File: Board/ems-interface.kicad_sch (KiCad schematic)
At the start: 51 parts, among them J8 EMS, Q1 BC858, Q11 BC848, U2 LM393, U3 MP1584

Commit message: Minor fixes
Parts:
- C11: value 22u -> 47u
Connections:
- net BUCK_EN: now reaches R15.1, R16.2, U3.2 (EN)
- net BUCK_FREQ: now reaches R13.1, U3.6 (FREQ)
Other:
- note added: "3.3 V"
- moved on the sheet: C10, C11, C12, C13, C9, D10, L3, R13, R14, R17, R18, U3

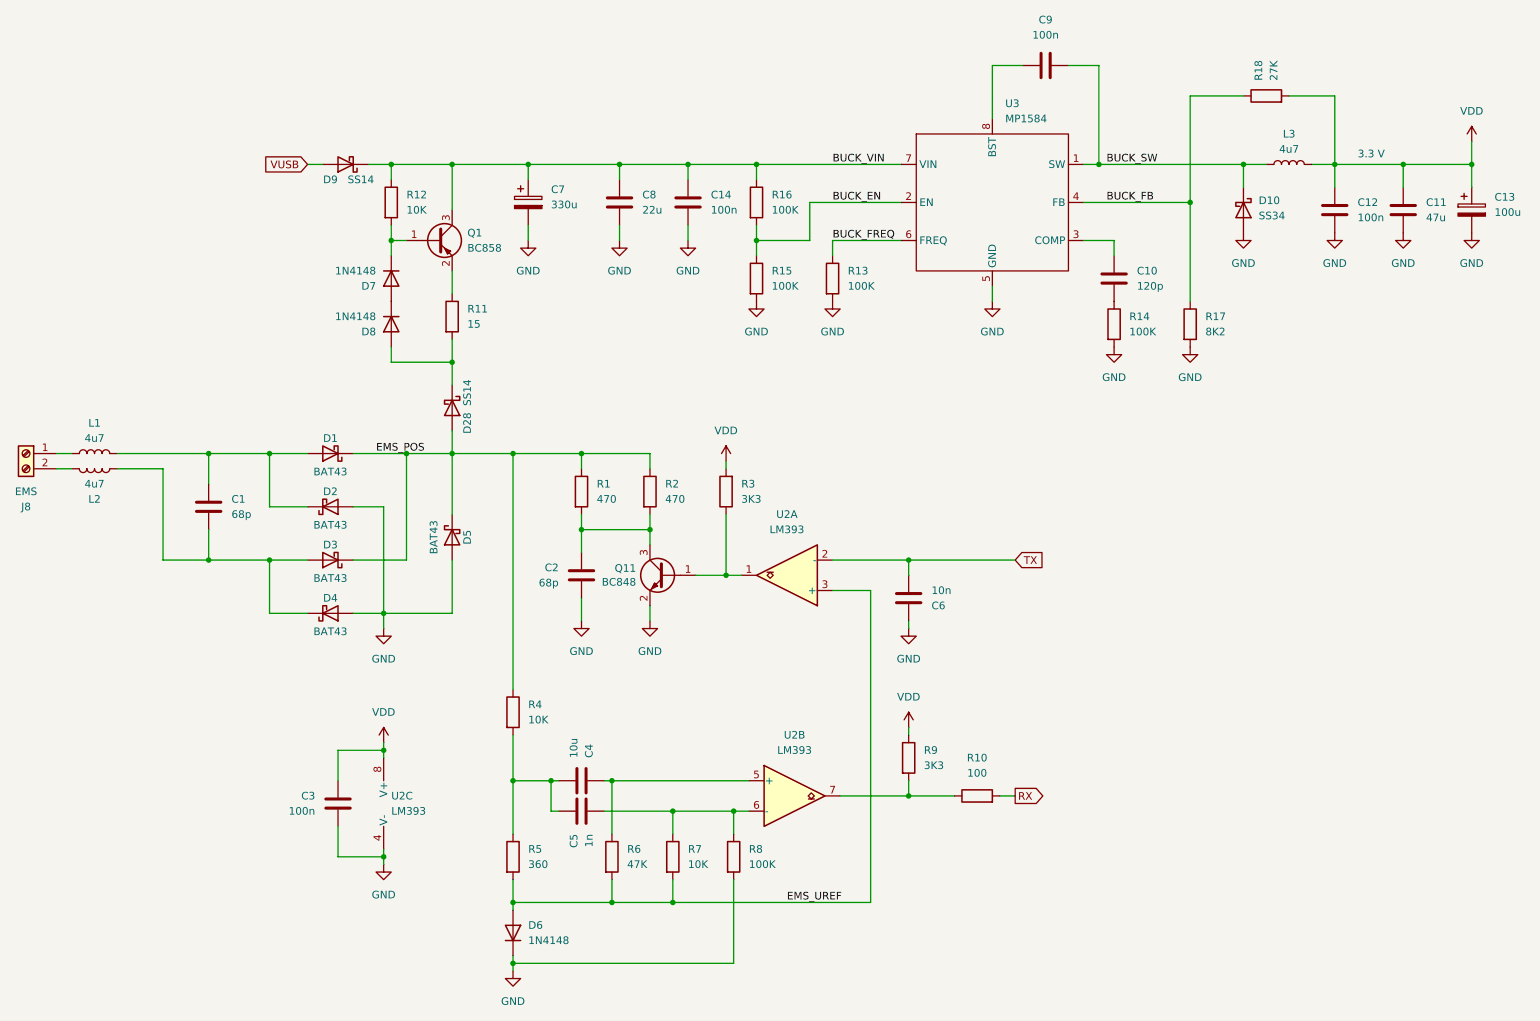
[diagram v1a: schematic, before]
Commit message: Fixes values
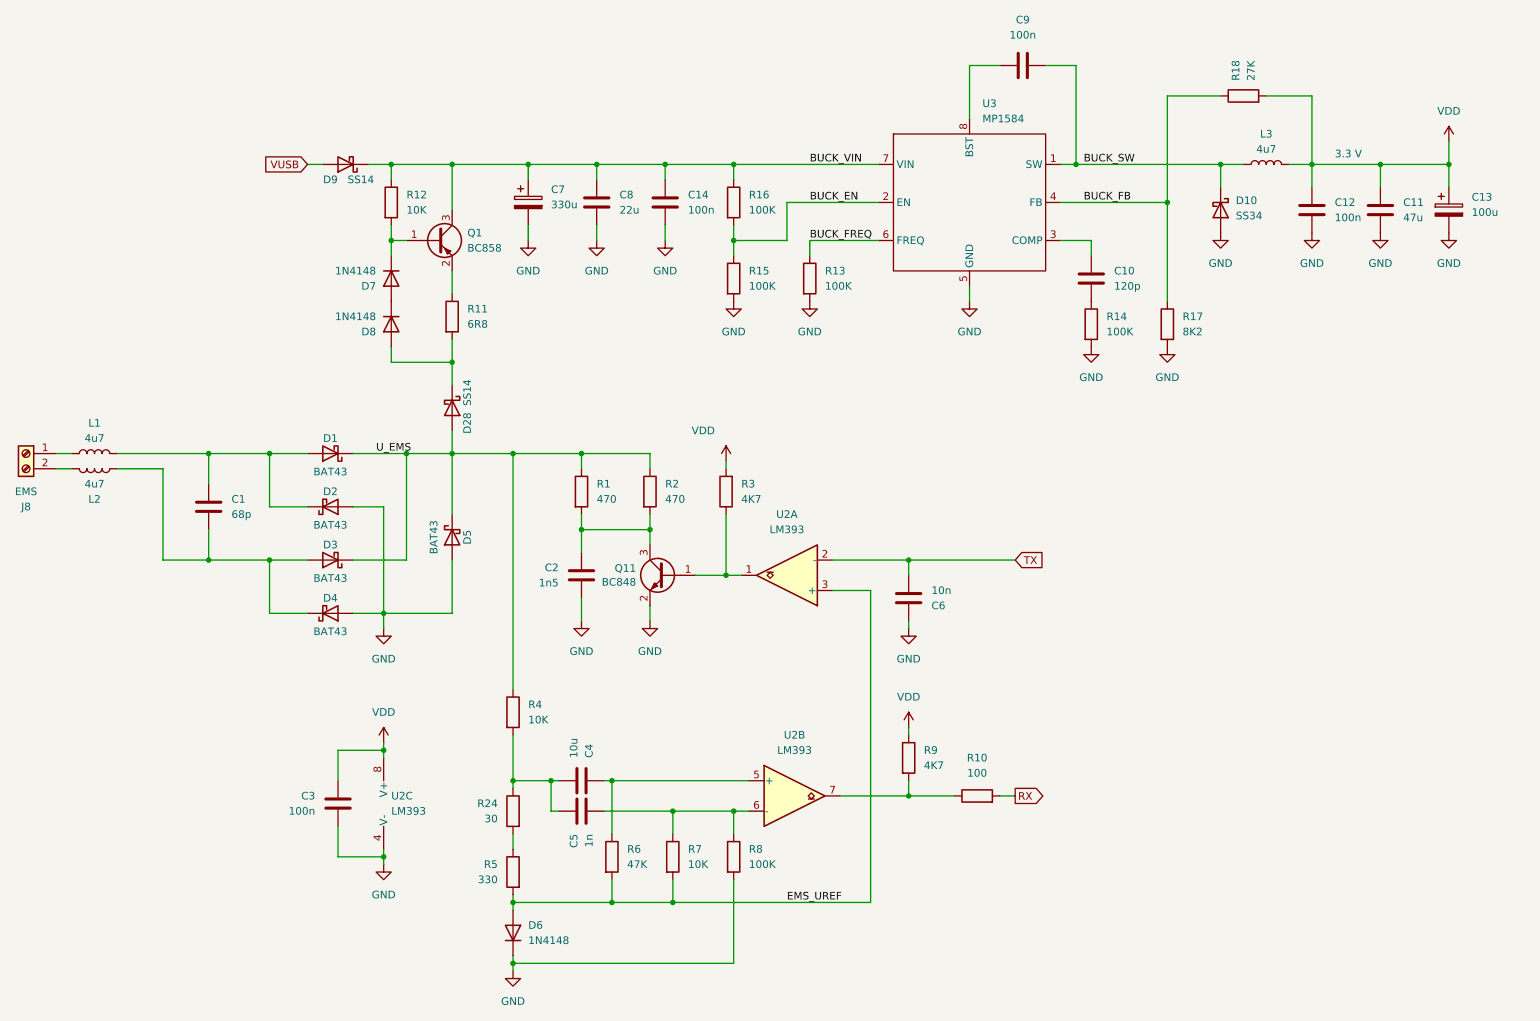
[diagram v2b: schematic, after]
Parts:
- added R24: 30, Resistor_SMD:R_0805_2012Metric, symbol Device:R
- C2: value 68p -> 1n5
- R11: value 15 -> 6R8
- R3, R9: value 3K3 -> 4K7
- R5: value 360 -> 330
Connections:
- net at C4.2, C5.1, R4.2: now also R24.1; no longer R5.1
- net EMS_POS renamed U_EMS
- new net: R24.2, R5.1
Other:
- moved on the sheet: C10, C11, C12, C13, C14, C8, C9, D10, L3, R13, R14, R15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

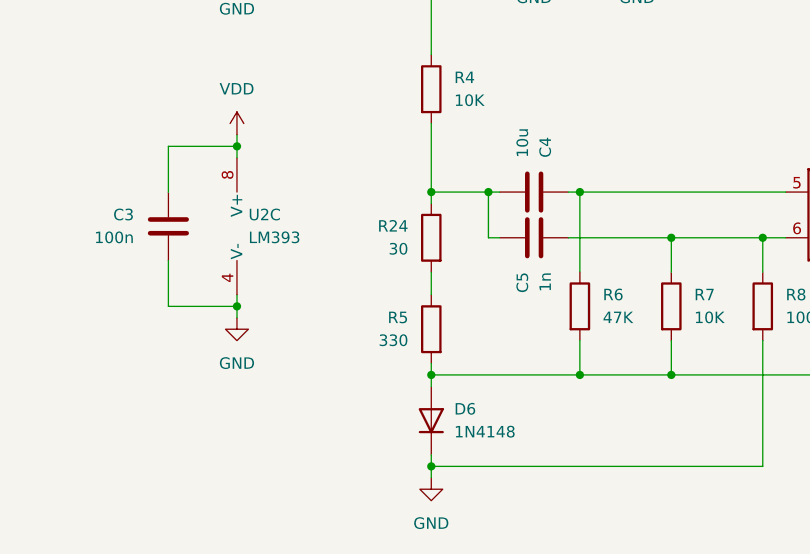
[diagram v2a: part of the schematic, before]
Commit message: Minor fixes and improvements. Changes board shape.
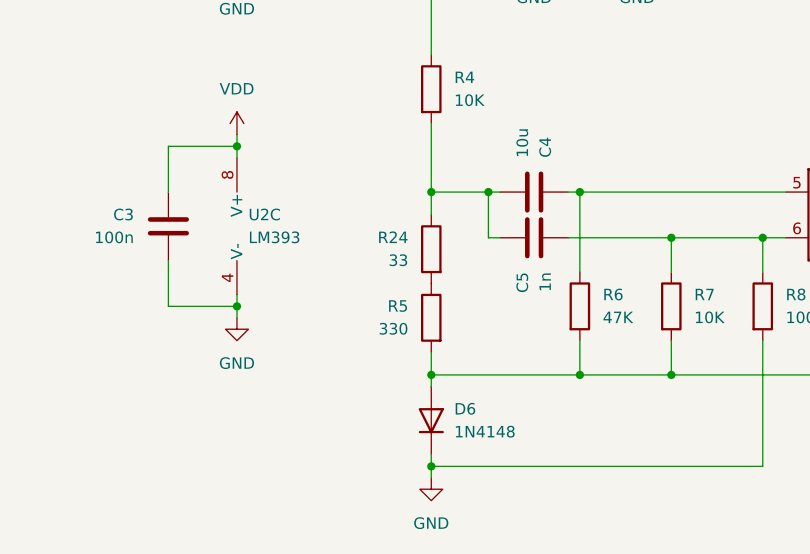
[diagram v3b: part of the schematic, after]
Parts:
- J8: footprint TerminalBlock:TerminalBlock_Altech_AK300-2_P5.00mm -> TerminalBlock_Altech:Altech_AK100_1x02_P5.00mm
- R24: value 30 -> 33
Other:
- moved on the sheet: R5
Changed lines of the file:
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@@
 	)
 	(junction
+		(at 104.14 156.21)
+		(diameter 0)
+		(color 0 0 0 0)
+	)
+	(junction
 		(at 248.92 53.34)
 		(diameter 0)
@@
 	)
 	(junction
-		(at 104.14 156.21)
-		(diameter 0)
-		(color 0 0 0 0)
-	)
-	(junction
 		(at 130.81 176.53)
 		(diameter 0)
@@
 	(wire
 		(pts
+			(xy 104.14 156.21) (xy 104.14 158.75)
+		)
+		(stroke
+			(width 0)
+			(type default)
+		)
+	)
+	(wire
+		(pts
 			(xy 163.83 124.46) (xy 163.83 176.53)
 		)
@@
 	(wire
 		(pts
-			(xy 104.14 175.26) (xy 104.14 176.53)
+			(xy 104.14 173.99) (xy 104.14 176.53)
 		)
 		(stroke
@@
 	(wire
 		(pts
-			(xy 104.14 156.21) (xy 104.14 157.48)
-		)
-		(stroke
-			(width 0)
-			(type default)
-		)
-	)
-	(wire
-		(pts
 			(xy 213.36 59.69) (xy 213.36 76.2)
 		)
@@
 	(wire
 		(pts
-			(xy 104.14 165.1) (xy 104.14 167.64)
-		)
-		(stroke
-			(width 0)
-			(type default)
-		)
-	)
-	(wire
-		(pts
 			(xy 180.34 36.83) (xy 185.42 36.83)
 		)
@@
 	(symbol
 		(lib_id "Device:R")
-		(at 104.14 171.45 0)
+		(at 104.14 170.18 0)
 		(mirror y)
 		(unit 1)
@@
 		(dnp no)
 		(property "Reference" "R5"
-			(at 101.6 170.1799 0)
+			(at 101.6 168.9099 0)
 			(effects
 				(font
@@
 		)
 		(property "Value" "330"
-			(at 101.6 172.7199 0)
+			(at 101.6 171.4499 0)
 			(effects
 				(font
@@
 		)
 		(property "Footprint" "Resistor_SMD:R_0805_2012Metric"
-			(at 105.918 171.45 90)
+			(at 105.918 170.18 90)
 			(effects
 				(font
@@
 		)
 		(property "Datasheet" "~"
-			(at 104.14 171.45 0)
+			(at 104.14 170.18 0)
 			(effects
 				(font
@@
 		)
 		(property "Description" "Resistor"
-			(at 104.14 171.45 0)
+			(at 104.14 170.18 0)
 			(effects
 				(font
@@
 	)
 	(symbol
-		(lib_id "Device:R")
-		(at 104.14 161.29 0)
-		(mirror y)
-		(unit 1)
-		(exclude_from_sim no)
-		(in_bom yes)
-		(on_board yes)
-		(dnp no)
-		(property "Reference" "R24"
-			(at 101.6 160.0199 0)
-			(effects
-				(font
-					(size 1.27 1.27)
-				)
-				(justify left)
-			)
-		)
-		(property "Value" "30"
-			(at 101.6 162.5599 0)
-			(effects
-				(font
-					(size 1.27 1.27)
-				)
-				(justify left)
-			)
-		)
-		(property "Footprint" "Resistor_SMD:R_0805_2012Metric"
-			(at 105.918 161.29 90)
-			(effects
-				(font
-					(size 1.27 1.27)
-				)
-				(hide yes)
-			)
-		)
-		(property "Datasheet" "~"
-			(at 104.14 161.29 0)
-			(effects
-				(font
-					(size 1.27 1.27)
-				)
-				(hide yes)
-			)
-		)
-		(property "Description" "Resistor"
-			(at 104.14 161.29 0)
-			(effects
-				(font
-					(size 1.27 1.27)
-				)
-				(hide yes)
-			)
-		)
-		(pin "1"
-		)
-		(pin "2"
-		)
-		(instances
-			(project "Mini-EMS-ESP"
-				(path "/20733457-9944-4316-ad39-5a8b057f497f/61ccb107-b821-45d5-b4c1-418cacc613b5"
-					(reference "R24")
-					(unit 1)
-				)
-			)
-		)
-	)
-	(symbol
 		(lib_id "Comparator:LM393")
 		(at 151.13 158.75 0)
@@
 	(symbol
 		(lib_id "Device:R")
+		(at 104.14 162.56 0)
+		(mirror y)
+		(unit 1)
+		(exclude_from_sim no)
+		(in_bom yes)
+		(on_board yes)
+		(dnp no)
+		(property "Reference" "R24"
+			(at 101.6 161.2899 0)
+			(effects
+				(font
+					(size 1.27 1.27)
+				)
+				(justify left)
+			)
+		)
+		(property "Value" "33"
+			(at 101.6 163.8299 0)
+			(effects
+				(font
+					(size 1.27 1.27)
+				)
+				(justify left)
+			)
+		)
+		(property "Footprint" "Resistor_SMD:R_0805_2012Metric"
+			(at 105.918 162.56 90)
+			(effects
+				(font
+					(size 1.27 1.27)
+				)
+				(hide yes)
+			)
+		)
+		(property "Datasheet" "~"
+			(at 104.14 162.56 0)
+			(effects
+				(font
+					(size 1.27 1.27)
+				)
+				(hide yes)
+			)
+		)
+		(property "Description" "Resistor"
+			(at 104.14 162.56 0)
+			(effects
+				(font
+					(size 1.27 1.27)
+				)
+				(hide yes)
+			)
+		)
+		(pin "1"
+		)
+		(pin "2"
+		)
+		(instances
+			(project "Mini-EMS-ESP"
+				(path "/20733457-9944-4316-ad39-5a8b057f497f/61ccb107-b821-45d5-b4c1-418cacc613b5"
+					(reference "R24")
+					(unit 1)
+				)
+			)
+		)
+	)
+	(symbol
+		(lib_id "Device:R")
 		(at 153.67 72.39 0)
 		(unit 1)
@@
 			)
 		)
-		(property "Footprint" "TerminalBlock:TerminalBlock_Altech_AK300-2_P5.00mm"
+		(property "Footprint" "TerminalBlock_Altech:Altech_AK100_1x02_P5.00mm"
 			(at 22.86 101.6 0)
 			(effects

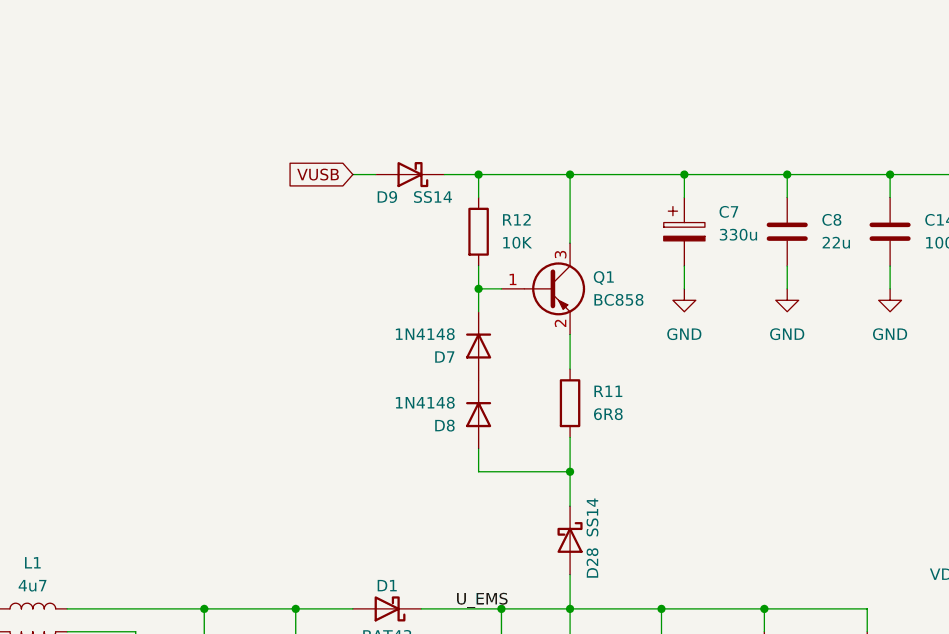
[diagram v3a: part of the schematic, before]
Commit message: Fixes constant current circuit.
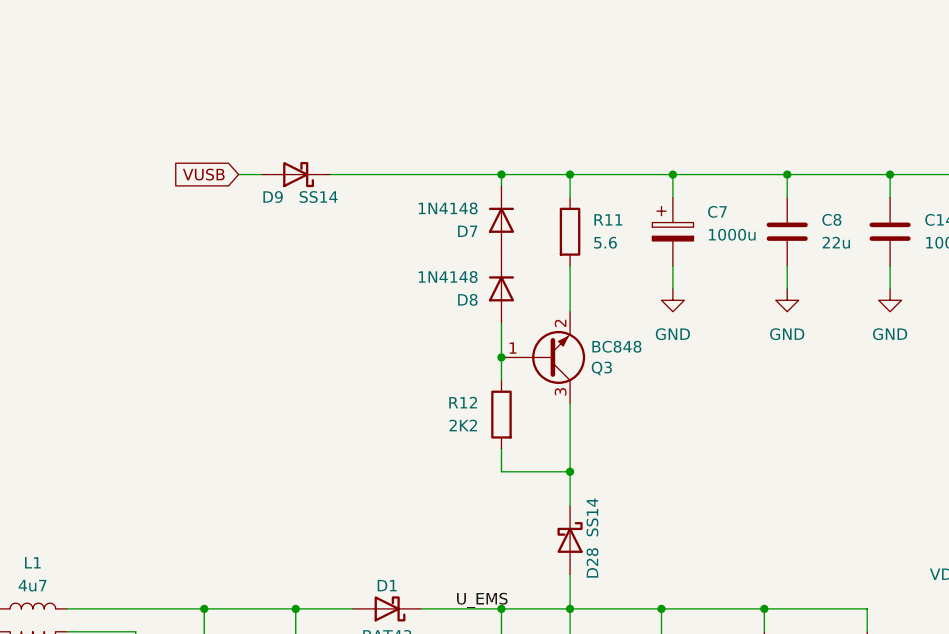
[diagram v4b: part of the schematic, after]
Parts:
- removed Q1: BC858, Package_TO_SOT_SMD:SOT-23, symbol Transistor_BJT:BC858
- added Q3: BC848, Package_TO_SOT_SMD:SOT-23, symbol Transistor_BJT:BC850
- C7: value 330u -> 1000u; footprint Capacitor_SMD:CP_Elec_8x10.5 -> Capacitor_SMD:CP_Elec_10x10.5
- R11: value 6R8 -> 5.6
- R12: value 10K -> 2K2
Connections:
- net BUCK_VIN: now also D7.1 (K), R11.1; no longer R12.1
- net at R12.2: now also D28.1 (K), Q3.3 (C); no longer D7.1 (K)
- new net: D8.2 (A), Q3.1 (B), R12.1
- new net: Q3.2 (E), R11.2
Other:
- moved on the sheet: C7, D7, D8, D9, R11, R12
